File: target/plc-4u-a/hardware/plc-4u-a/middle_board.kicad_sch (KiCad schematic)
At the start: 44 parts, among them J16 I2C, J17 TA_C, J18 X leds btns, J20 Valve leds, J21 Leak sensors, J22 Valve control in, J25 S3 S5 LEDs, J26 S4 S6 LEDs, J31 S3BTN, J32 S4BTN, J33 S5BTN, J34 S6BTN, J35 PWR_OUT, J36 Sensors AB, J37 Sensors CD, J38 PWR_OUT, J39 Leak sensors, J45 TB_C, J46 TC_C, J47 TD_C, J49 S1 S2 LEDs, J50 S1 S2 BTNS, J53 X0 IN, J54 X9 IN, Q10 MMBT3904, Q7 MMBT3904, Q8 MMBT3904, Q9 MMBT3904, U17 PC817, U18 PC817, U19 PC817, U20 PC817, U21 PC817, U8 PC817

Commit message: update
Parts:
- removed J53: X0 IN, Connector_PinHeader_2.54mm:PinHeader_1x02_P2.54mm_Vertical, symbol Connector:Conn_01x02_Male
- added C2: C_Polarized, Capacitor_SMD:C_1812_4532Metric, symbol Device:C_Polarized
- added J51: X0, Connector_PinHeader_2.54mm:PinHeader_1x01_P2.54mm_Vertical, symbol Connector:Conn_01x01_Male
- added J56: U17 OUT, Connector_PinHeader_2.54mm:PinHeader_1x02_P2.54mm_Vertical, symbol Connector:Conn_01x02_Male
- added J57: U8 OUT, Connector_PinHeader_2.54mm:PinHeader_1x02_P2.54mm_Vertical, symbol Connector:Conn_01x02_Male
- added J60: GND, Connector_PinHeader_2.54mm:PinHeader_1x01_P2.54mm_Vertical, symbol Connector:Conn_01x01_Male
- added J62: VCC, Connector_PinHeader_2.54mm:PinHeader_1x01_P2.54mm_Vertical, symbol Connector:Conn_01x01_Male
- added J64: SIM800, Connector_PinHeader_2.54mm:PinHeader_1x06_P2.54mm_Vertical, symbol Connector:Conn_01x06_Male
- added J65: RES_IN, TerminalBlock_Phoenix:TerminalBlock_Phoenix_MKDS-1,5-2-5.08_1x02_P5.08mm_Horizontal, symbol Connector:Screw_Terminal_01x02
- added J66: SELF_PWR_IN, TerminalBlock_Phoenix:TerminalBlock_Phoenix_MKDS-1,5-2-5.08_1x02_P5.08mm_Horizontal, symbol Connector:Screw_Terminal_01x02
- added J68: VDD VSS, Connector_PinHeader_2.54mm:PinHeader_1x02_P2.54mm_Vertical, symbol Connector:Conn_01x02_Male
- added J70, J77: VDD, Connector_PinHeader_2.54mm:PinHeader_1x01_P2.54mm_Vertical, symbol Connector:Conn_01x01_Male
- added J71: RESERVED_OUT, Connector_PinHeader_2.54mm:PinHeader_1x01_P2.54mm_Vertical, symbol Connector:Conn_01x01_Male
- added J72, J73, J74: VSS, Connector_PinHeader_2.54mm:PinHeader_1x01_P2.54mm_Vertical, symbol Connector:Conn_01x01_Male
- added J80, J82: NC, Connector_PinHeader_2.54mm:PinHeader_1x01_P2.54mm_Vertical, symbol Connector:Conn_01x01_Male
- added R62: R, Resistor_SMD:R_0805_2012Metric, symbol Device:R
- added R63: R, Resistor_THT:R_Axial_DIN0309_L9.0mm_D3.2mm_P5.08mm_Vertical, symbol Device:R
- added U23: PC817, Package_DIP:DIP-4_W7.62mm, symbol Isolator:PC817
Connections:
- net SCL: now also J64.2 (Pin_2)
- net VCC: now also J35.1 (Pin_1), J38.1 (Pin_1), J62.1 (Pin_1)
- net VSS: now also C2.2, J56.1 (Pin_1), J57.1 (Pin_1), J64.1 (Pin_1), J66.2 (Pin_2), J68.1 (Pin_1), J73.1 (Pin_1), J74.1 (Pin_1)
- net X0: now also J51.1 (Pin_1)
- net GND: now reaches J38.2 (Pin_2)
- net GND: now also J35.2 (Pin_2), J60.1 (Pin_1)
- net PC2: now reaches U8.4
- net PC2: now also J57.2 (Pin_2)
- net PA0: now reaches U17.4
- net PA0: now also J56.2 (Pin_2)
- net SDA renamed RXD
- net RXD: now also J64.3 (Pin_3)
- new net: J72.1 (Pin_1), U23.3
- new net: R63.2, U23.1
- new net: J71.1 (Pin_1), R62.1, U23.4
- new net RESET: J64.4 (Pin_4)
- new net RES_IN_H: J65.1 (Pin_1), R63.1
- new net RES_IN_L: J65.2 (Pin_2), U23.2
- new net VDD: C2.1, J64.5 (Pin_5), J66.1 (Pin_1), J68.2 (Pin_2), J70.1 (Pin_1), J77.1 (Pin_1), R62.2

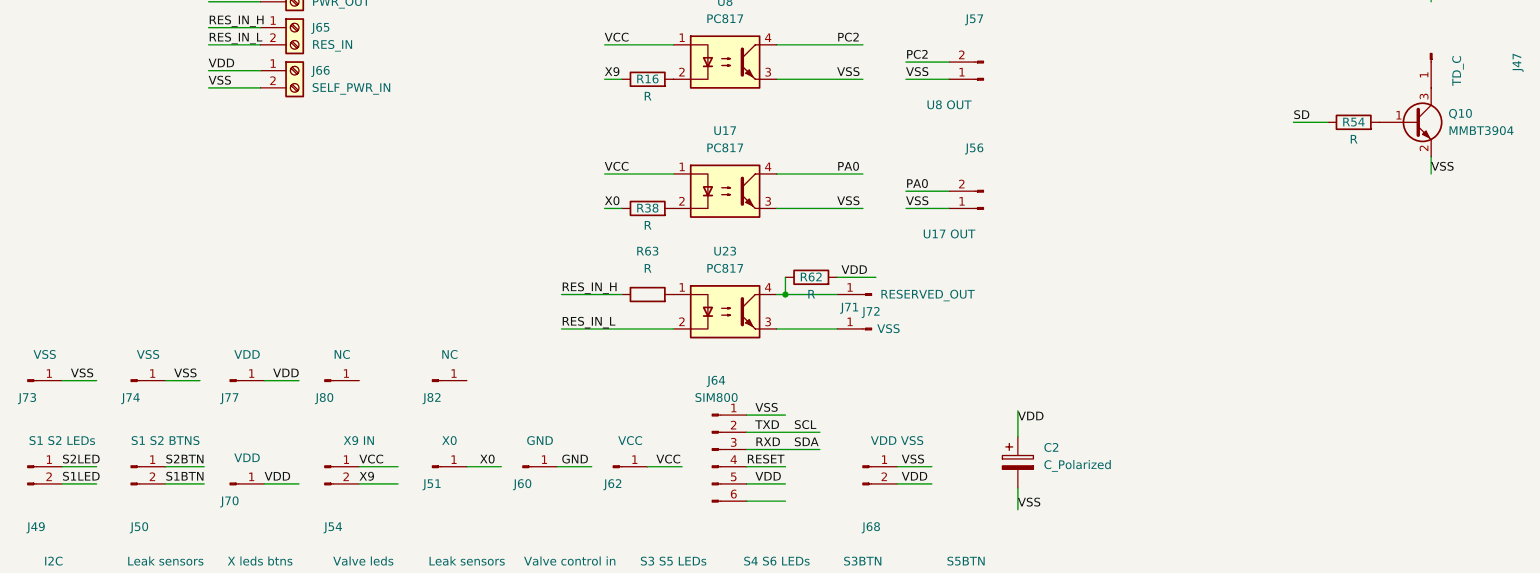
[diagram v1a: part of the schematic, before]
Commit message: plc-4u-a board += leds
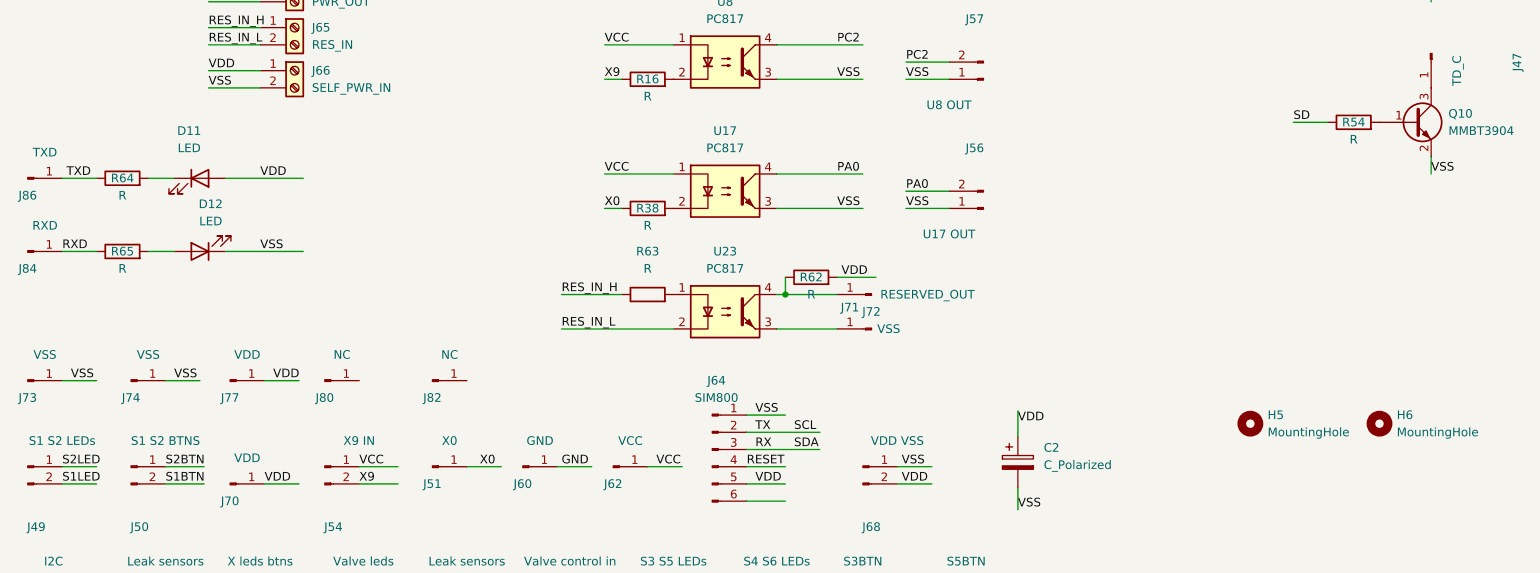
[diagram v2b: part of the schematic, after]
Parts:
- added D11, D12: LED, LED_THT:LED_D3.0mm, symbol Device:LED
- added H5, H6: MountingHole, MountingHole:MountingHole_3.2mm_M3, symbol Mechanical:MountingHole
- added J84: RXD, Connector_PinHeader_2.54mm:PinHeader_1x01_P2.54mm_Vertical, symbol Connector:Conn_01x01_Male
- added J86: TXD, Connector_PinHeader_2.54mm:PinHeader_1x01_P2.54mm_Vertical, symbol Connector:Conn_01x01_Male
- added R64, R65: R, Resistor_SMD:R_0805_2012Metric, symbol Device:R
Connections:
- net RXD: now also J84.1 (Pin_1), R65.1; no longer J16.2 (Pin_2), J64.3 (Pin_3)
- net VDD: now also D11.2 (A)
- net VSS: now also D12.1 (K)
- new net: D12.2 (A), R65.2
- new net: D11.1 (K), R64.2
- new net RX: J16.2 (Pin_2), J64.3 (Pin_3)
- new net TXD: J86.1 (Pin_1), R64.1
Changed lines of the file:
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@@
+    (stroke (width 0) (type default) (color 0 0 0 0))
+  )
+  (wire (pts (xy 34.29 122.555) (xy 38.1 122.555))
     (stroke (width 0) (type default) (color 0 0 0 0))
   )
@@
     (stroke (width 0) (type default) (color 0 0 0 0))
   )
+  (wire (pts (xy 45.72 133.35) (xy 57.15 133.35))
+    (stroke (width 0) (type default) (color 0 0 0 0))
+  )
   (wire (pts (xy 223.52 68.58) (xy 223.52 71.12))
     (stroke (width 0) (type default) (color 0 0 0 0))
@@
     (stroke (width 0) (type default) (color 0 0 0 0))
   )
+  (wire (pts (xy 45.72 122.555) (xy 57.15 122.555))
+    (stroke (width 0) (type default) (color 0 0 0 0))
+  )
   (wire (pts (xy 127 53.34) (xy 139.7 53.34))
     (stroke (width 0) (type default) (color 0 0 0 0))
@@
     (stroke (width 0) (type default) (color 0 0 0 0))
   )
+  (wire (pts (xy 21.59 122.555) (xy 26.67 122.555))
+    (stroke (width 0) (type default) (color 0 0 0 0))
+  )
   (wire (pts (xy 36.83 190.5) (xy 41.91 190.5))
     (stroke (width 0) (type default) (color 0 0 0 0))
@@
     (stroke (width 0) (type default) (color 0 0 0 0))
   )
+  (wire (pts (xy 34.29 133.35) (xy 38.1 133.35))
+    (stroke (width 0) (type default) (color 0 0 0 0))
+  )
   (wire (pts (xy 43.18 90.17) (xy 50.8 90.17))
     (stroke (width 0) (type default) (color 0 0 0 0))
@@
     (stroke (width 0) (type default) (color 0 0 0 0))
   )
+  (wire (pts (xy 21.59 133.35) (xy 26.67 133.35))
+    (stroke (width 0) (type default) (color 0 0 0 0))
+  )
   (wire (pts (xy 203.2 88.9) (xy 208.28 88.9))
     (stroke (width 0) (type default) (color 0 0 0 0))
@@
     (effects (font (size 1.27 1.27)) (justify left bottom))
   )
+  (label "RXD" (at 21.59 133.35 0)
+    (effects (font (size 1.27 1.27)) (justify left bottom))
+  )
   (label "SDA" (at 129.54 162.56 0)
     (effects (font (size 1.27 1.27)) (justify left bottom))
@@
     (effects (font (size 1.27 1.27)) (justify left bottom))
   )
+  (label "VDD" (at 50.8 122.555 0)
+    (effects (font (size 1.27 1.27)) (justify left bottom))
+  )
   (label "PD2" (at 62.23 50.8 0)
     (effects (font (size 1.27 1.27)) (justify left bottom))
@@
     (effects (font (size 1.27 1.27)) (justify left bottom))
   )
-  (label "TXD" (at 123.825 160.02 0)
+  (label "TX" (at 123.825 160.02 0)
     (effects (font (size 1.27 1.27)) (justify left bottom))
   )
@@
     (effects (font (size 1.27 1.27)) (justify left bottom))
   )
-  (label "RXD" (at 123.825 162.56 0)
+  (label "RX" (at 123.825 162.56 0)
     (effects (font (size 1.27 1.27)) (justify left bottom))
   )
@@
     (effects (font (size 1.27 1.27)) (justify left bottom))
   )
+  (label "VSS" (at 50.8 133.35 0)
+    (effects (font (size 1.27 1.27)) (justify left bottom))
+  )
   (label "PB4" (at 31.75 44.45 0)
     (effects (font (size 1.27 1.27)) (justify left bottom))
@@
   )
   (label "SB" (at 39.37 187.96 0)
+    (effects (font (size 1.27 1.27)) (justify left bottom))
+  )
+  (label "TXD" (at 22.225 122.555 0)
     (effects (font (size 1.27 1.27)) (justify left bottom))
   )
@@
     (pin "2")
   )
+  (symbol (lib_id "Connector:Conn_01x01_Male") (at 16.51 122.555 0) (unit 1)
+    (in_bom yes) (on_board yes)
+    (property "Reference" "J86" (id 0) (at 16.51 125.095 0))
+    (property "Value" "TXD" (id 1) (at 19.05 118.745 0))
+    (property "Footprint" "Connector_PinHeader_2.54mm:PinHeader_1x01_P2.54mm_Vertical" (id 2) (at 16.51 122.555 0)
+      (effects (font (size 1.27 1.27)) hide)
+    )
+    (property "Datasheet" "~" (id 3) (at 16.51 122.555 0)
+      (effects (font (size 1.27 1.27)) hide)
+    )
+    (pin "1")
+  )
   (symbol (lib_id "Connector:Conn_01x01_Male") (at 46.355 167.64 0) (unit 1)
     (in_bom yes) (on_board yes)
@@
     (pin "1")
   )
+  (symbol (lib_id "Device:LED") (at 41.91 133.35 180) (unit 1)
+    (in_bom yes) (on_board yes) (fields_autoplaced)
+    (property "Reference" "D12" (id 0) (at 43.4975 126.365 0))
+    (property "Value" "LED" (id 1) (at 43.4975 128.905 0))
+    (property "Footprint" "LED_THT:LED_D3.0mm" (id 2) (at 41.91 133.35 0)
+      (effects (font (size 1.27 1.27)) hide)
+    )
+    (property "Datasheet" "~" (id 3) (at 41.91 133.35 0)
+      (effects (font (size 1.27 1.27)) hide)
+    )
+    (pin "1")
+    (pin "2")
+  )
   (symbol (lib_id "Connector:Conn_01x02_Male") (at 157.48 107.95 180) (unit 1)
     (in_bom yes) (on_board yes)
@@
     (pin "1")
     (pin "2")
+  )
+  (symbol (lib_id "Mechanical:MountingHole") (at 196.85 158.75 0) (unit 1)
+    (in_bom yes) (on_board yes) (fields_autoplaced)
+    (property "Reference" "H5" (id 0) (at 199.39 157.4799 0)
+      (effects (font (size 1.27 1.27)) (justify left))
+    )
+    (property "Value" "MountingHole" (id 1) (at 199.39 160.0199 0)
+      (effects (font (size 1.27 1.27)) (justify left))
+    )
+    (property "Footprint" "MountingHole:MountingHole_3.2mm_M3" (id 2) (at 196.85 158.75 0)
+      (effects (font (size 1.27 1.27)) hide)
+    )
+    (property "Datasheet" "~" (id 3) (at 196.85 158.75 0)
+      (effects (font (size 1.27 1.27)) hide)
+    )
   )
   (symbol (lib_id "Connector:Conn_01x04_Male") (at 60.96 185.42 0) (unit 1)
@@
     (pin "1")
   )
+  (symbol (lib_id "Device:R") (at 30.48 133.35 90) (unit 1)
+    (in_bom yes) (on_board yes)
+    (property "Reference" "R65" (id 0) (at 30.48 133.35 90))
+    (property "Value" "R" (id 1) (at 30.48 135.89 90))
+    (property "Footprint" "Resistor_SMD:R_0805_2012Metric" (id 2) (at 30.48 135.128 90)
+      (effects (font (size 1.27 1.27)) hide)
+    )
+    (property "Datasheet" "~" (id 3) (at 30.48 133.35 0)
+      (effects (font (size 1.27 1.27)) hide)
+    )
+    (pin "1")
+    (pin "2")
+  )
   (symbol (lib_id "Connector:Conn_01x01_Male") (at 223.52 53.34 270) (unit 1)
     (in_bom yes) (on_board yes)
@@
     (pin "4")
   )
+  (symbol (lib_id "Connector:Conn_01x01_Male") (at 16.51 133.35 0) (unit 1)
+    (in_bom yes) (on_board yes)
+    (property "Reference" "J84" (id 0) (at 16.51 135.89 0))
+    (property "Value" "RXD" (id 1) (at 19.05 129.54 0))
+    (property "Footprint" "Connector_PinHeader_2.54mm:PinHeader_1x01_P2.54mm_Vertical" (id 2) (at 16.51 133.35 0)
+      (effects (font (size 1.27 1.27)) hide)
+    )
+    (property "Datasheet" "~" (id 3) (at 16.51 133.35 0)
+      (effects (font (size 1.27 1.27)) hide)
+    )
+    (pin "1")
+  )
   (symbol (lib_id "Connector:Conn_01x02_Male") (at 31.75 165.1 0) (unit 1)
     (in_bom yes) (on_board yes)
@@
     (pin "1")
   )
+  (symbol (lib_id "Device:R") (at 30.48 122.555 90) (unit 1)
+    (in_bom yes) (on_board yes)
+    (property "Reference" "R64" (id 0) (at 30.48 122.555 90))
+    (property "Value" "R" (id 1) (at 30.48 125.095 90))
+    (property "Footprint" "Resistor_SMD:R_0805_2012Metric" (id 2) (at 30.48 124.333 90)
+      (effects (font (size 1.27 1.27)) hide)
+    )
+    (property "Datasheet" "~" (id 3) (at 30.48 122.555 0)
+      (effects (font (size 1.27 1.27)) hide)
+    )
+    (pin "1")
+    (pin "2")
+  )
   (symbol (lib_id "Connector:Conn_01x04_Male") (at 31.75 185.42 0) (unit 1)
     (in_bom yes) (on_board yes)
@@
     (pin "1")
   )
+  (symbol (lib_id "Mechanical:MountingHole") (at 215.9 158.75 0) (unit 1)
+    (in_bom yes) (on_board yes) (fields_autoplaced)
+    (property "Reference" "H6" (id 0) (at 218.44 157.4799 0)
+      (effects (font (size 1.27 1.27)) (justify left))
+    )
+    (property "Value" "MountingHole" (id 1) (at 218.44 160.0199 0)
+      (effects (font (size 1.27 1.27)) (justify left))
+    )
+    (property "Footprint" "MountingHole:MountingHole_3.2mm_M3" (id 2) (at 215.9 158.75 0)
+      (effects (font (size 1.27 1.27)) hide)
+    )
+    (property "Datasheet" "~" (id 3) (at 215.9 158.75 0)
+      (effects (font (size 1.27 1.27)) hide)
+    )
+  )
   (symbol (lib_id "Device:R") (at 212.09 114.3 90) (unit 1)
     (in_bom yes) (on_board yes)
@@
       (effects (font (size 1.27 1.27)) hide)
     )
+    (pin "1")
+    (pin "2")
+  )
+  (symbol (lib_id "Device:LED") (at 41.91 122.555 0) (unit 1)
+    (in_bom yes) (on_board yes) (fields_autoplaced)
+    (property "Reference" "D11" (id 0) (at 40.3225 115.57 0))
+    (property "Value" "LED" (id 1) (at 40.3225 118.11 0))
+    (property "Footprint" "LED_THT:LED_D3.0mm" (id 2) (at 41.91 122.555 0)
+      (effects (font (size 1.27 1.27)) hide)
+    )
+    (property "Datasheet" "~" (id 3) (at 41.91 122.555 0)
+      (effects (font (size 1.27 1.27)) hide)
+    )

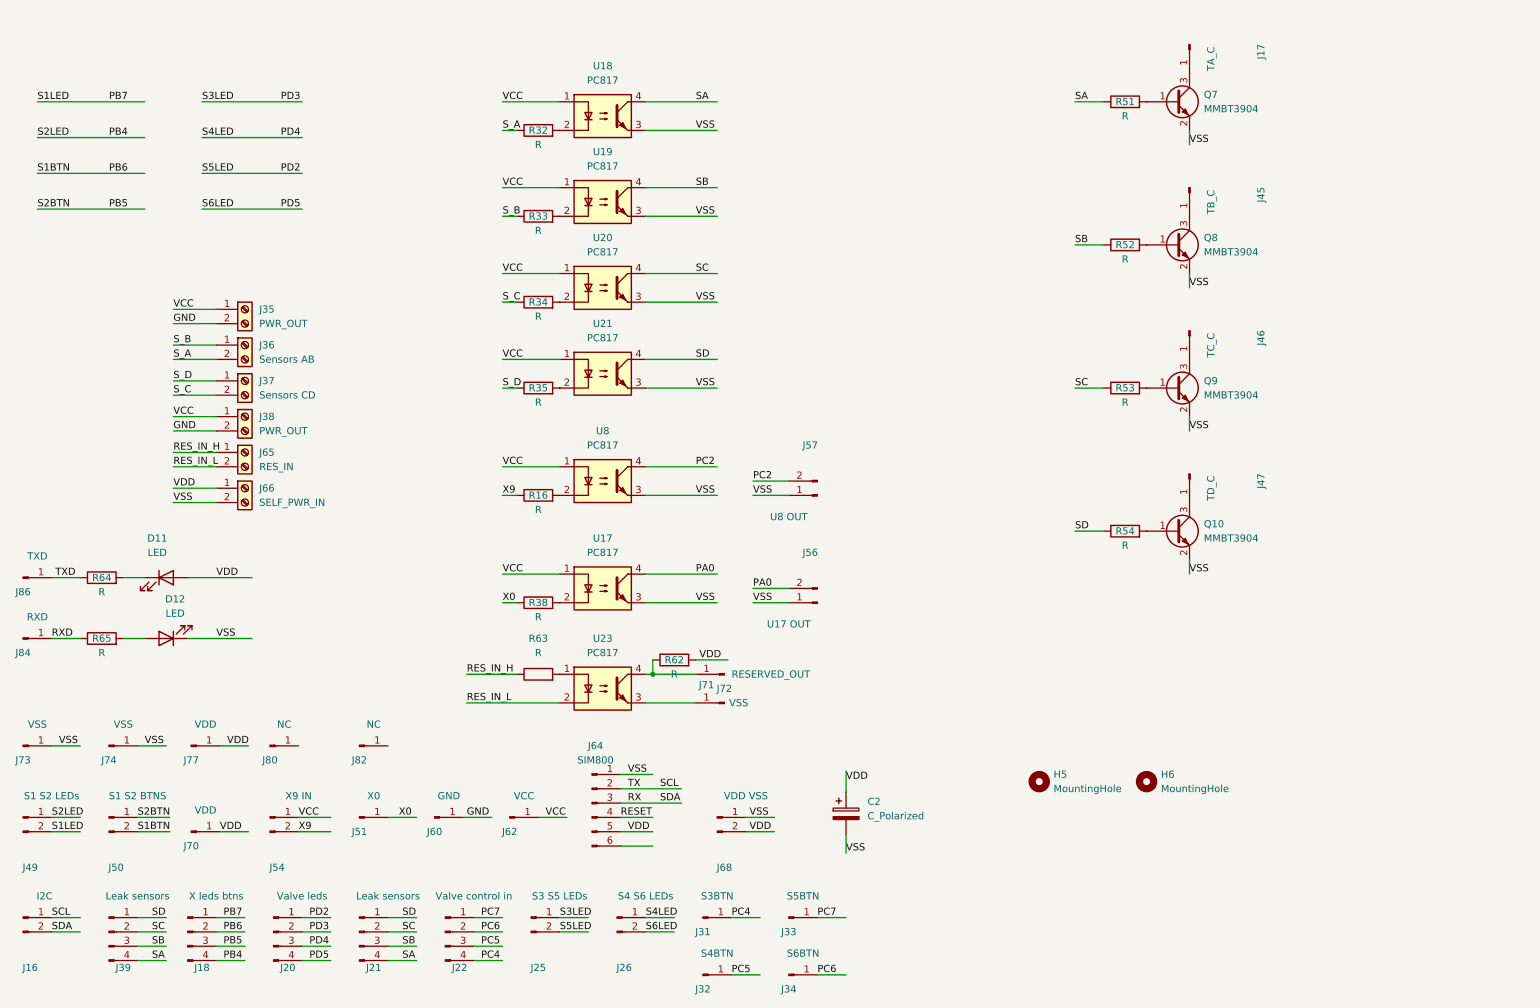
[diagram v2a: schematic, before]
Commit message: plc4u-a: main-retained-register (preparing for buzzer)
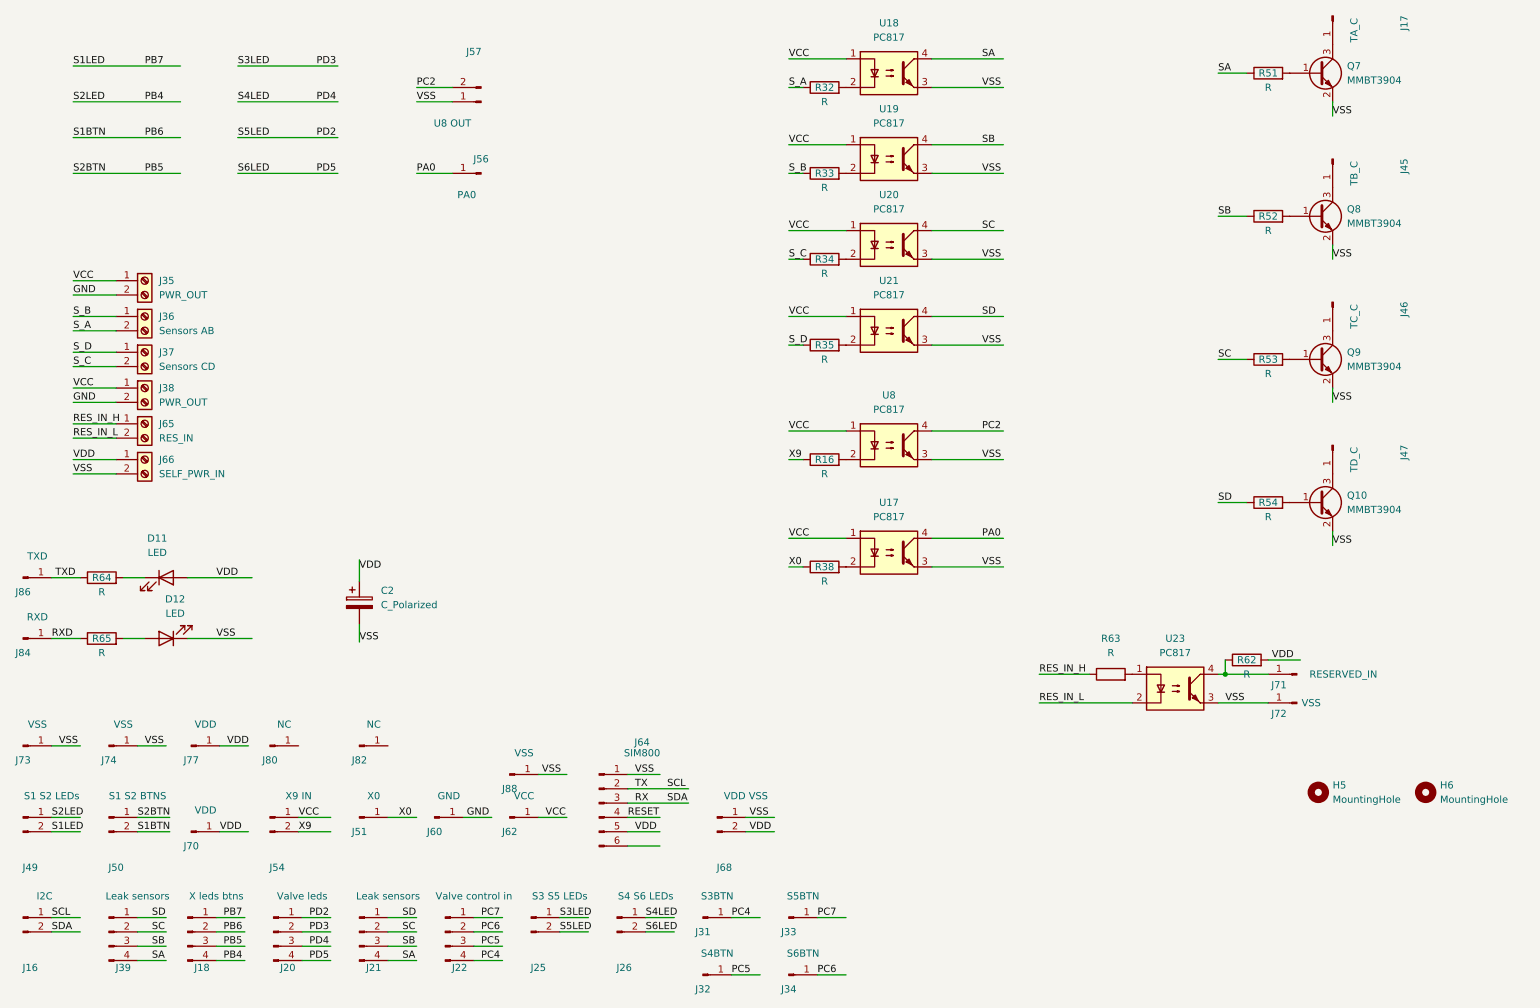
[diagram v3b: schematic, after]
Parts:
- removed J56: U17 OUT, Connector_PinHeader_2.54mm:PinHeader_1x02_P2.54mm_Vertical, symbol Connector:Conn_01x02_Male
- added J56: PA0, Connector_PinHeader_2.54mm:PinHeader_1x01_P2.54mm_Vertical, symbol Connector:Conn_01x01_Male
- added J88: VSS, Connector_PinHeader_2.54mm:PinHeader_1x01_P2.54mm_Vertical, symbol Connector:Conn_01x01_Male
- J71: value RESERVED_OUT -> RESERVED_IN
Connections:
- net PA0: now also J56.1 (Pin_1)
- net VSS: now also J72.1 (Pin_1), U23.3, J88.1 (Pin_1)
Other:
- moved on the sheet: C2, H5, H6, J17, J35, J36, J37, J38, J45, J46, J47, J57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
